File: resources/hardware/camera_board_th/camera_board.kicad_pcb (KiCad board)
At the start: 2 copper layers, 10 parts, among them P1 CONN_01X02

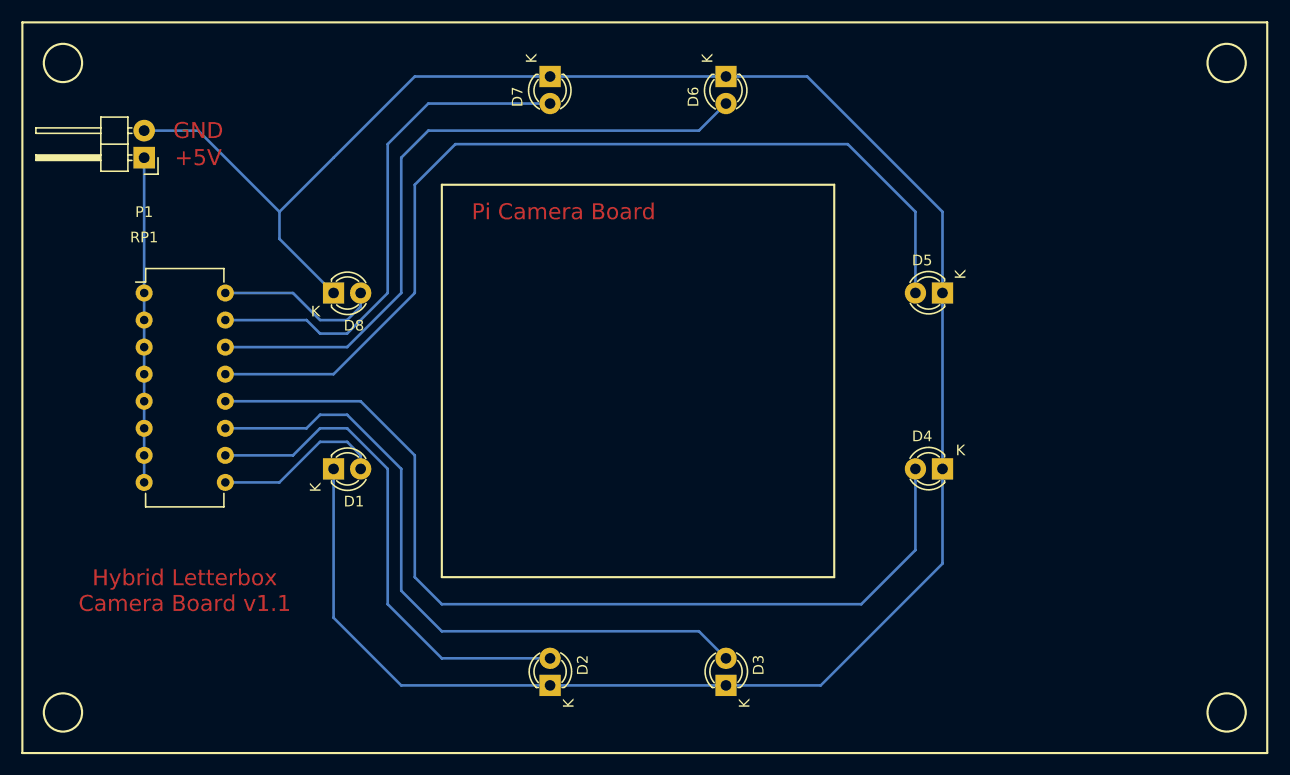
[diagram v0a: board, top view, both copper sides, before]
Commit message: added lasercut sketches for outer frame
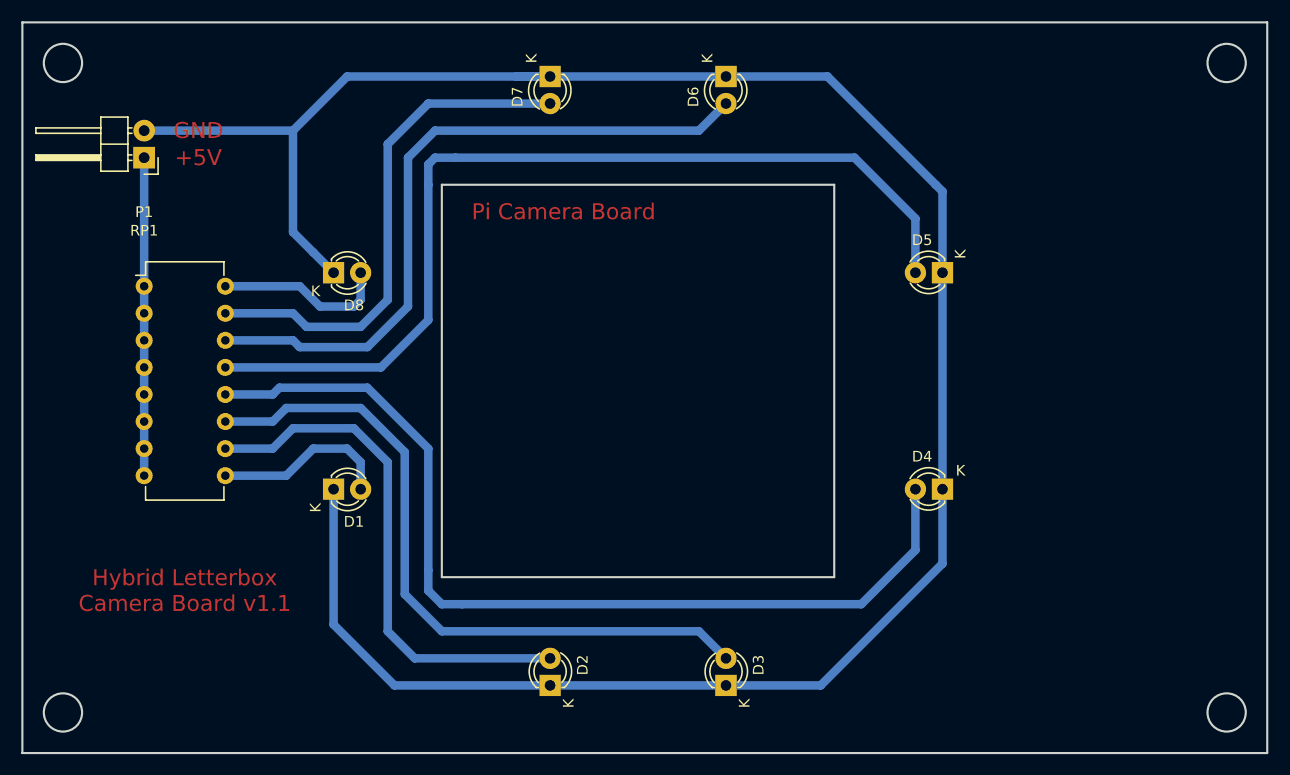
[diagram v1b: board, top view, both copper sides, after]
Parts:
- moved D5 1.91 mm to (153.7, 79.4)
- moved D8 1.91 mm to (96.5, 79.4)
- moved D1 1.90 mm to (96.5, 99.7)
- moved D4 1.90 mm to (153.7, 99.7)
- moved RP1 0.64 mm to (78.7, 80.6)
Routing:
- net +5V: track 30.5 -> 32.4 mm
- net GND: track 209.8 -> 211.5 mm
- net Net-(D2-Pad2): track 47.9 -> 49.5 mm
- net Net-(D3-Pad2): track 63.7 -> 65.1 mm
- net Net-(D6-Pad2): track 63.9 -> 64.9 mm
- net Net-(D5-Pad2): track 89.9 -> 88.9 mm
- net Net-(D8-Pad2): track 15.5 -> 16.3 mm
- net Net-(D1-Pad2): track 16.1 -> 16.8 mm
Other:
- board outline added: 116.8 x 68.6 mm
- net class Default: clearance 0.2 -> 0.8; trace_width 0.25 -> 0.8; via_dia 0.6 -> 1.4; via_drill 0.4 -> 0.8
- rule trace_clearance: 0.2 -> 0.8
- rule trace_min: 0.2 -> 0.8
- rule via_min_drill: 0.3 -> 0.8
- rule via_min_size: 0.4 -> 1.4
